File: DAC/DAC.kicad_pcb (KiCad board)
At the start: 4 copper layers, 53.8 x 36.7 mm, 39 parts, among them J1 Conn_01x06, J2 Conn_01x06, J3 Conn_01x06_Male, J4 Conn_01x02, J5 Conn_01x03_Male, J6 Conn_01x03_Male, J7 Conn_01x02, SW1 SW_Push, U1 TPS73633DBV, U2 PCM5242RHB

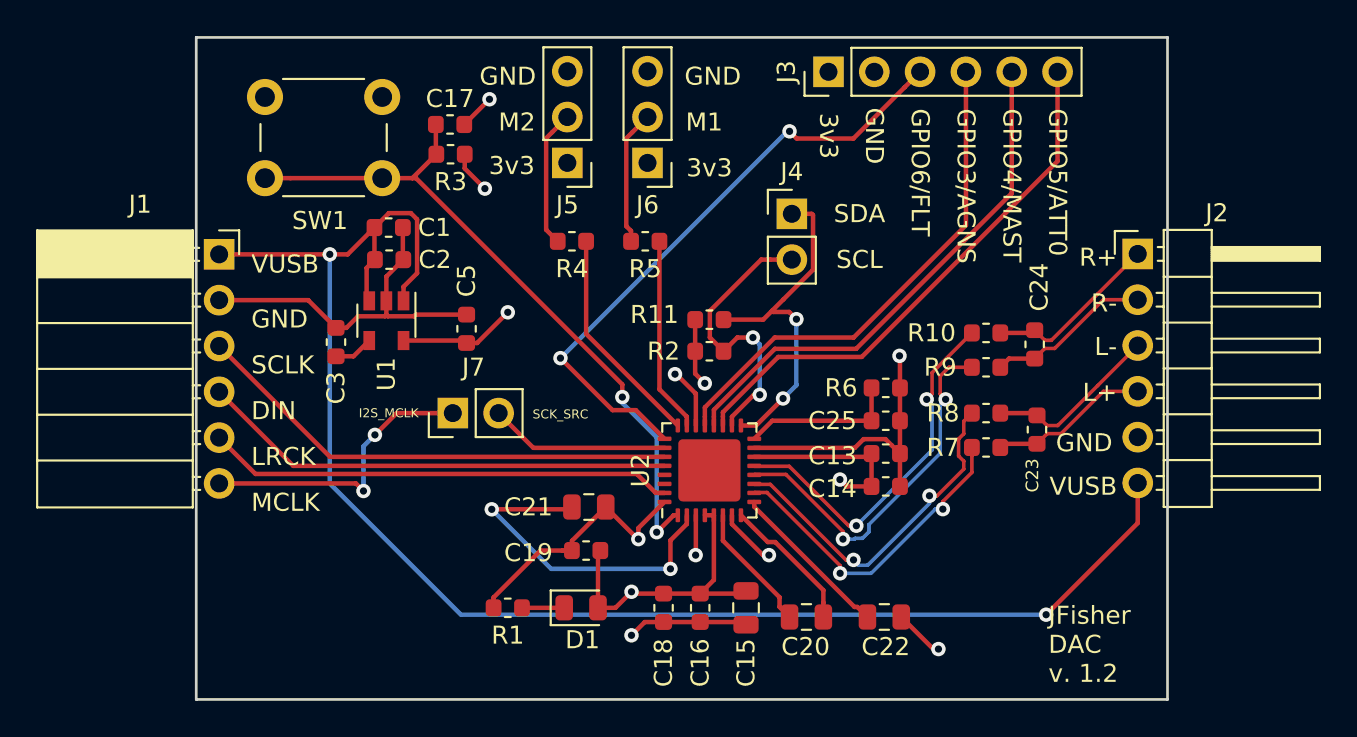
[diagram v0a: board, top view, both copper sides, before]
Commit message: Add analysis python code for windowing
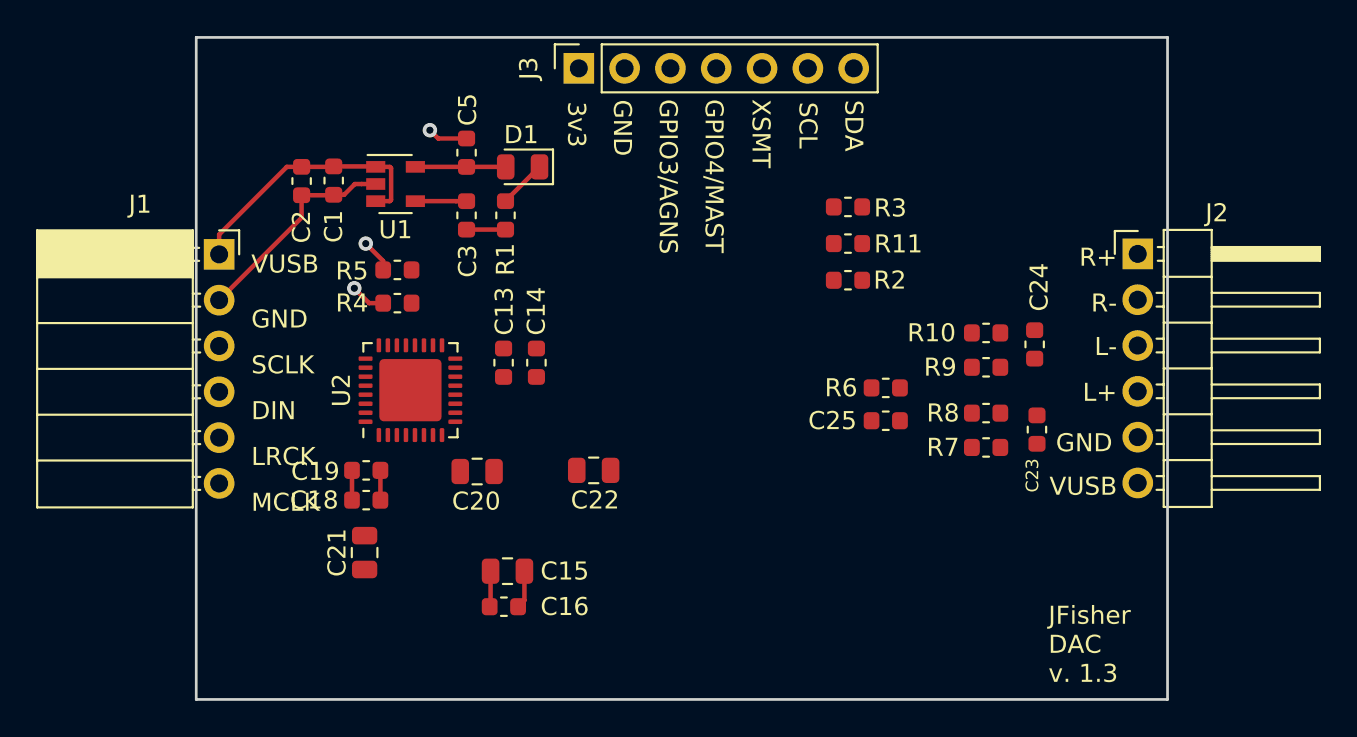
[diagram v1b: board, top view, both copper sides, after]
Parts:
- removed C17: 0.1uF, Capacitor_SMD:C_0603_1608Metric
- removed J4, J7: Conn_01x02, Connector_PinHeader_2.54mm:PinHeader_1x02_P2.54mm_Vertical
- removed J5, J6: Conn_01x03_Male, Connector_PinHeader_2.54mm:PinHeader_1x03_P2.54mm_Vertical
- removed SW1: SW_Push, Button_Switch_THT:SW_PUSH_6mm
- J3: value Conn_01x06_Male -> Conn_01x07_Male; footprint Connector_PinHeader_2.54mm:PinHeader_1x06_P2.54mm_Vertical -> Connector_PinSocket_2.54mm:PinSocket_1x07_P2.54mm_Vertical
- R3: value 10k -> 4.99k
- moved D1 24.7 mm to (129.9, 39.6), turned to 180 degrees
- moved R3 22.2 mm to (147.9, 41.8)
- moved C13 21.8 mm to (128.8, 50.4), turned to 90 degrees
- moved R1 21.8 mm to (128.9, 42.3), turned to 270 degrees
- moved C14 20.5 mm to (130.6, 50.4), turned to 90 degrees
- moved C20 20.0 mm to (127.3, 56.5)
- moved C22 18.0 mm to (133.8, 56.4)
- moved C18 17.5 mm to (121.2, 58.0), turned to 180 degrees
- moved U2 17.2 mm to (123.6, 51.9)
- moved J3 13.8 mm to (133.0, 34.1)
- moved R5 13.8 mm to (122.9, 45.3)
- moved C15 13.4 mm to (129.0, 62.0), turned to 0 degrees
- moved C19 13.0 mm to (121.2, 56.4)
- moved C21 12.7 mm to (121.1, 60.9), turned to 270 degrees
- moved C16 10.9 mm to (128.8, 63.9), turned to 0 degrees
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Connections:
- J1 pad 6: I2S_MCLK -> GPIO5_ATT0
- J3 pad 3: GPIO6_FLT -> GPIO3_AGNS
- J3 pad 4: GPIO3_AGNS -> GPIO4_MAST
- J3 pad 5: GPIO4_MAST -> XSMT
- J3 pad 6: GPIO5_ATT0 -> SCL_MC_ATT1
- R3 pad 1: Net-(C17-Pad1) -> XSMT
- R4 pad 2: Net-(J5-Pad2) -> +3V3
- R5 pad 2: Net-(J6-Pad2) -> GND
- U2 pad 1: Net-(C17-Pad1) -> XSMT
- U2 pad 26: I2S_SCK_SRC -> GPIO6_FLT
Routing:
- net VUSB: track 86.1 -> 14.9 mm, vias 2 -> 0
- net GND: track 70.5 -> 22.1 mm, vias 8 -> 2
- net Net-(C17-Pad1): track 38.6 -> 0.00 mm, vias 2 -> 0
- net GPIO6_FLT: track 34.5 -> 0.00 mm, vias 2 -> 0
- net GPIO5_ATT0: track 30.0 -> 0.00 mm
- net +3V3: track 40.0 -> 10.6 mm, vias 5 -> 1
- net GPIO4_MAST: track 29.1 -> 0.00 mm
- net GPIO3_AGNS: track 28.2 -> 0.00 mm
- net I2S_SCLK: track 27.2 -> 0.00 mm
- net I2S_DIN: track 26.4 -> 0.00 mm
- net I2S_LRCK: track 26.0 -> 0.00 mm
- net OUTR_N: track 20.7 -> 0.00 mm, vias 2 -> 0
- net OUTR_P: track 20.6 -> 0.00 mm, vias 2 -> 0
- net SDA_MOSI_ATT2: track 19.5 -> 0.00 mm, vias 2 -> 0
- net OUTL_N: track 19.5 -> 0.00 mm, vias 2 -> 0
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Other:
- board text added: "JFisher DAC v. 1.3"
- board text added: "XSMT"
- board text removed: "GPIO5/ATT0"
- board text removed: "GPIO6/FLT"
- board text removed: "I2S_MCLK"
- board text removed: "JFisher DAC v. 1.2"
- board text removed: "M1"
- board text removed: "M2"
- board text removed: "SCK_SRC"
